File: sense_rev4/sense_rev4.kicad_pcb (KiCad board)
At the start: 2 copper layers, 68 x 52 mm, 46 parts, among them J1 Audio-Jack-4, P1 CONN_02X05, Q1 Q_PMOS_DGS, SW1 SW_SPST, U1 MDBT42Q, U2 PIR, U3 TLV8802, U4 MCP4012T-503E/CH, Y1 Crystal

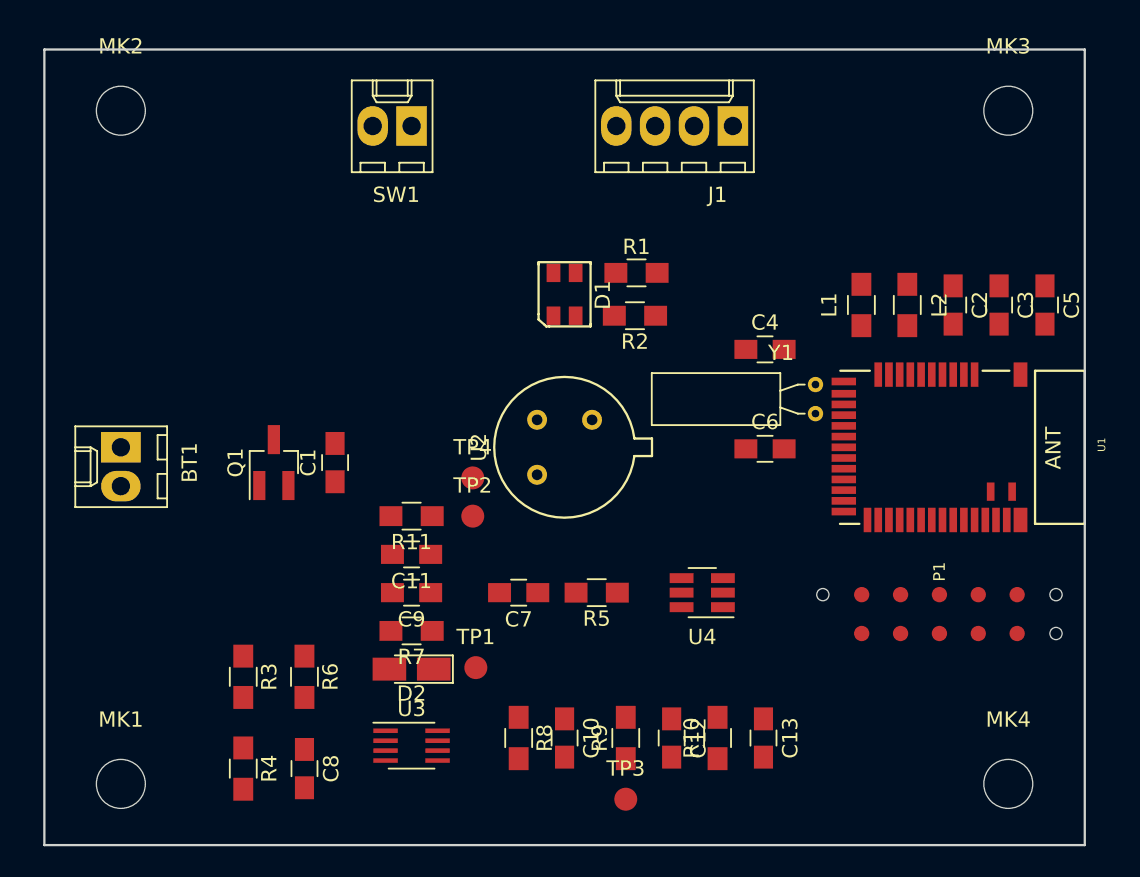
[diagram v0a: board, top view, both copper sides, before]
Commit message: Adds Schematics and PCB Layout files
PCB routing completed.
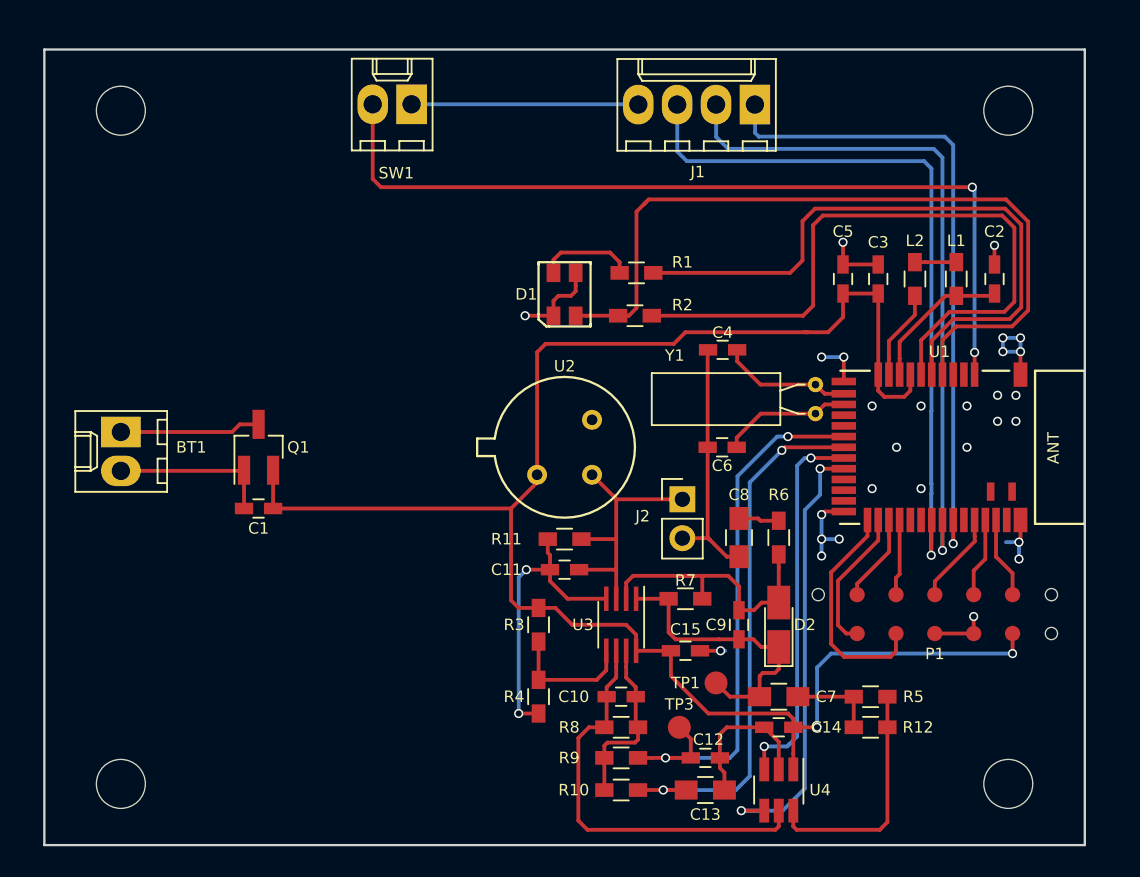
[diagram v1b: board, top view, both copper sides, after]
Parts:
- removed TP2, TP4: TEST, Measurement_Points:Measurement_Point_Round-SMD-Pad_Small
- added C14: 0.1uF, Capacitors_SMD:C_0603_HandSoldering, F.Cu at (152.0, 123.3)
- added C15: 0.1uF, Capacitors_SMD:C_0603_HandSoldering, F.Cu at (145.9, 118.3)
- added J2: Conn_01x02, Pin_Headers:Pin_Header_Straight_1x02_Pitch2.54mm, F.Cu at (145.7, 108.4)
- added R12: 33k, Resistors_SMD:R_0603_HandSoldering, F.Cu at (158.0, 123.3)
- C1, C10, C11, C2, C3, C4, C5, C6, C9: footprint Capacitors_SMD:C_0805_HandSoldering -> Capacitors_SMD:C_0603_HandSoldering
- C12: value 100nF -> 100pF; footprint Capacitors_SMD:C_0805_HandSoldering -> Capacitors_SMD:C_0603_HandSoldering
- C13, C7, C8: value 10uF -> 22uF
- L1, L2: footprint Inductors_SMD:L_0805_HandSoldering -> Inductors_SMD:L_0603_HandSoldering
- R1, R2: value R -> 22E; footprint Resistors_SMD:R_0805_HandSoldering -> Resistors_SMD:R_0603_HandSoldering
- R10, R6, R9: value 47k -> 33k; footprint Resistors_SMD:R_0805_HandSoldering -> Resistors_SMD:R_0603_HandSoldering
- R11, R3, R4, R7, R8: footprint Resistors_SMD:R_0805_HandSoldering -> Resistors_SMD:R_0603_HandSoldering
- R5: value 10k -> 33k; footprint Resistors_SMD:R_0805_HandSoldering -> Resistors_SMD:R_0603_HandSoldering
- moved R6 32.3 mm to (152.0, 110.9), turned to 90 degrees
- moved C8 32.2 mm to (149.4, 110.9)
- moved D2 24.2 mm to (152.0, 116.6), turned to 90 degrees
- moved C9 21.5 mm to (149.4, 116.6), turned to 90 degrees
- moved R4 19.9 mm to (136.3, 121.3)
- moved R3 19.6 mm to (136.3, 116.6)
- moved R5 19.1 mm to (158.0, 121.3)
- moved C7 18.3 mm to (152.0, 121.3)
- moved R7 18.0 mm to (145.9, 114.9), turned to 0 degrees
- moved U3 15.8 mm to (141.7, 116.6), turned to 270 degrees
- moved TP1 15.7 mm to (147.9, 120.4)
- moved U4 13.8 mm to (152.0, 127.4), turned to 270 degrees
- moved C5 13.3 mm to (156.2, 94.0)
- moved R11 10.1 mm to (138.0, 111.0)
- moved C11 10.0 mm to (138.0, 113.0)
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- renumbered MK1 to ?, MK2 to ?, MK3 to ?, MK4 to ?
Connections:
- P1 pad 10: GND -> /GPIO1
- P1 pad 2: /GPIO2 -> VDD
- P1 pad 4: VDD -> GND
- P1 pad 6: /GPIO1 -> GND
- P1 pad 8: /TX -> /GPIO2
- P1 pad 9: GND -> /TX
- R5 pad 1: Net-(R5-Pad1) -> Net-(R12-Pad1)
- U1 pad 17: /AMP_OFFSET -> /AMP_SIGNAL
- U1 pad 18: /AMP_SIGNAL -> /AMP_OFFSET
- U1 pad 2: Net-(U1-Pad2) -> /BUTTON
- U1 pad 25: /TRIGGER -> /GPIO2
- U1 pad 26: /FOCUS -> /GPIO1
- U1 pad 27: /AUDIO_JACK_IO -> /TX
- U1 pad 28: Net-(U1-Pad28) -> /RX
- U1 pad 3: /BUTTON -> Net-(U1-Pad3)
- U1 pad 31: /GPIO2 -> /AUDIO_JACK_IO
- U1 pad 32: /GPIO1 -> /FOCUS
- U1 pad 33: /TX -> /TRIGGER
- U1 pad 34: /RX -> Net-(U1-Pad34)
- U1 pad 4: /LED_RED -> Net-(U1-Pad4)
- U1 pad 5: /LED_GREEN -> /LED_SENSE
- U1 pad 6: /LED_SENSE -> /LED_RED
- U1 pad 7: Net-(U1-Pad7) -> /LED_GREEN
- U4 pad 5: Net-(R5-Pad1) -> Net-(C10-Pad2)
- U4 pad 6: Net-(C10-Pad2) -> Net-(R12-Pad1)
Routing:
- net VDD: track 0.00 -> 116.2 mm, vias 0 -> 2
- net GND: track 0.00 -> 105.0 mm, vias 0 -> 19
- net /BUTTON: track 0.00 -> 56.6 mm, vias 0 -> 2
- net /LED_SENSE: track 0.00 -> 51.7 mm
- net /AUDIO_JACK_IO: track 0.00 -> 47.8 mm, vias 0 -> 1
- net /FOCUS: track 0.00 -> 45.1 mm, vias 0 -> 1
- net /LED_GREEN: track 0.00 -> 44.0 mm
- net /TRIGGER: track 0.00 -> 42.7 mm, vias 0 -> 1
- net /LED_RED: track 0.00 -> 42.1 mm
- net /AMP_SIGNAL: track 0.00 -> 36.8 mm, vias 0 -> 2
- net /AMP_OFFSET: track 0.00 -> 35.5 mm, vias 0 -> 2
- net /MCP4012T_CS: track 0.00 -> 29.1 mm, vias 0 -> 2
- net Net-(C10-Pad2): track 0.00 -> 27.2 mm
- net /MCP4012T_U/d: track 0.00 -> 25.0 mm, vias 0 -> 2
- net /OUT_A: track 0.00 -> 19.4 mm
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- added copper zone on B.Cu, net GND

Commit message: Updated PCB Routing
PCB routing updated,
Appiko, OSHW and KiCAD logos added.
All component placement changed.
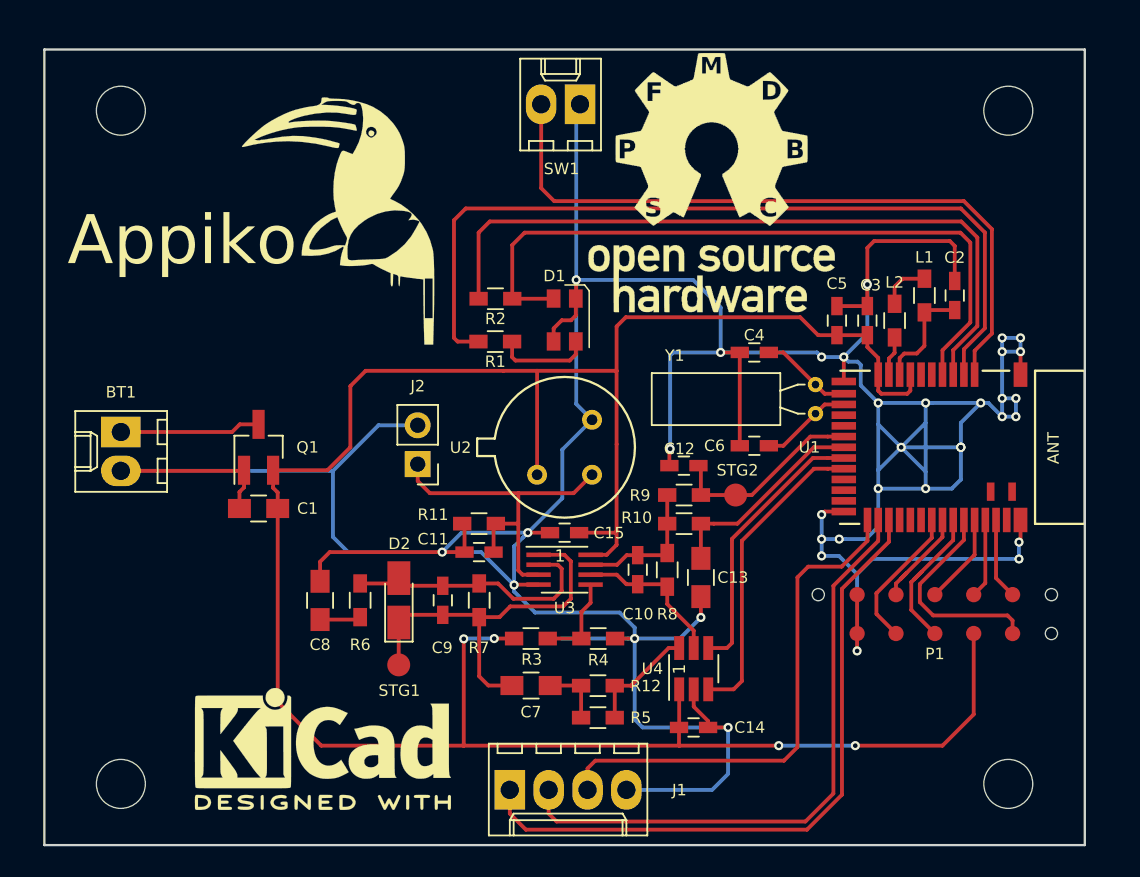
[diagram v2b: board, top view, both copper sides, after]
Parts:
- added ?: , sense_rev3_fp:LOGO, F.Cu at (123.2, 90.2)
- added ?: KiCad-Logo2_8mm_SilkScreen, sense_rev3_fp:KiCad-Logo2_8mm_SilkScreen, F.Cu at (122.2, 124.7)
- added G***: LOGO, sense_rev3_fp:OSHW1, F.Cu at (147.6, 87.7)
- C1: footprint Capacitors_SMD:C_0603_HandSoldering -> Capacitors_SMD:C_0805_HandSoldering
- moved J1 47.6 mm to (134.4, 127.4), turned to 0 degrees
- moved C8 27.7 mm to (122.0, 115.0), turned to 90 degrees
- moved R6 27.7 mm to (124.6, 115.0), turned to 270 degrees
- moved D2 24.9 mm to (127.2, 115.0)
- moved STG1 20.8 mm to (127.2, 119.2)
- moved C9 19.4 mm to (130.0, 115.0)
- moved C12 19.2 mm to (145.8, 106.2), turned to 0 degrees
- moved R12 18.0 mm to (140.2, 120.6)
- moved R10 17.9 mm to (145.8, 110.0)
- moved R5 17.9 mm to (140.2, 122.7)
- moved R9 17.7 mm to (145.8, 108.1)
- moved J2 17.5 mm to (128.4, 106.1), turned to 180 degrees
- moved C7 16.2 mm to (135.8, 120.6)
- moved STG2 15.6 mm to (149.2, 108.1)
- moved C13 13.9 mm to (146.9, 113.5), turned to 90 degrees
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- renumbered TP1 to STG1, TP3 to STG2
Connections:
- P1 pad 10: /GPIO1 -> GND
- P1 pad 2: VDD -> /TX
- P1 pad 4: GND -> VDD
- P1 pad 6: GND -> /GPIO1
- P1 pad 7: /RX -> /GPIO2
- P1 pad 8: /GPIO2 -> /RX
- P1 pad 9: /TX -> GND
- U1 pad 25: /GPIO2 -> /AUDIO_JACK_IO
- U1 pad 26: /GPIO1 -> /FOCUS
- U1 pad 27: /TX -> /TRIGGER
- U1 pad 28: /RX -> Net-(U1-Pad28)
- U1 pad 3: Net-(U1-Pad3) -> /LED_RED
- U1 pad 31: /AUDIO_JACK_IO -> /RX
- U1 pad 32: /FOCUS -> /GPIO2
- U1 pad 33: /TRIGGER -> /GPIO1
- U1 pad 34: Net-(U1-Pad34) -> /TX
- U1 pad 4: Net-(U1-Pad4) -> /LED_GREEN
- U1 pad 6: /LED_RED -> Net-(U1-Pad6)
- U1 pad 7: /LED_GREEN -> Net-(U1-Pad7)
- U4 pad 3: /MCP4012T_U/d -> /MCP4012T_CS
- U4 pad 4: /MCP4012T_CS -> /MCP4012T_U/d
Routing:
- net GND: track 105.0 -> 315.2 mm, vias 19 -> 35
- net VDD: track 116.2 -> 159.9 mm, vias 2 -> 4
- net /AMP_SIGNAL: track 36.8 -> 12.9 mm, vias 2 -> 0
- net /AMP_OFFSET: track 35.5 -> 13.7 mm, vias 2 -> 0
- net Net-(C10-Pad2): track 27.2 -> 10.1 mm
- net /AUDIO_JACK_IO: track 47.8 -> 33.7 mm, vias 1 -> 0
- net /LED_RED: track 42.1 -> 54.9 mm
- net /BUTTON: track 56.6 -> 46.0 mm, vias 2 -> 0
- net /MCP4012T_CS: track 29.1 -> 20.2 mm, vias 2 -> 0
- net /GPIO2: track 15.0 -> 6.65 mm
- net Net-(R12-Pad1): track 15.7 -> 7.32 mm
- net /TX: track 5.75 -> 14.0 mm
- net /MCP4012T_U/d: track 25.0 -> 18.0 mm, vias 2 -> 0
- net /OUT_A: track 19.4 -> 25.8 mm
- net /LED_SENSE: track 51.7 -> 46.1 mm
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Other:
- net class Default: via_drill 0.4 -> 0.35
- rule via_min_drill: 0.3 -> 0.2
- board text added: "1"

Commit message: Updates PCB files
Added notes in schematic, and changes few references in PCB file.
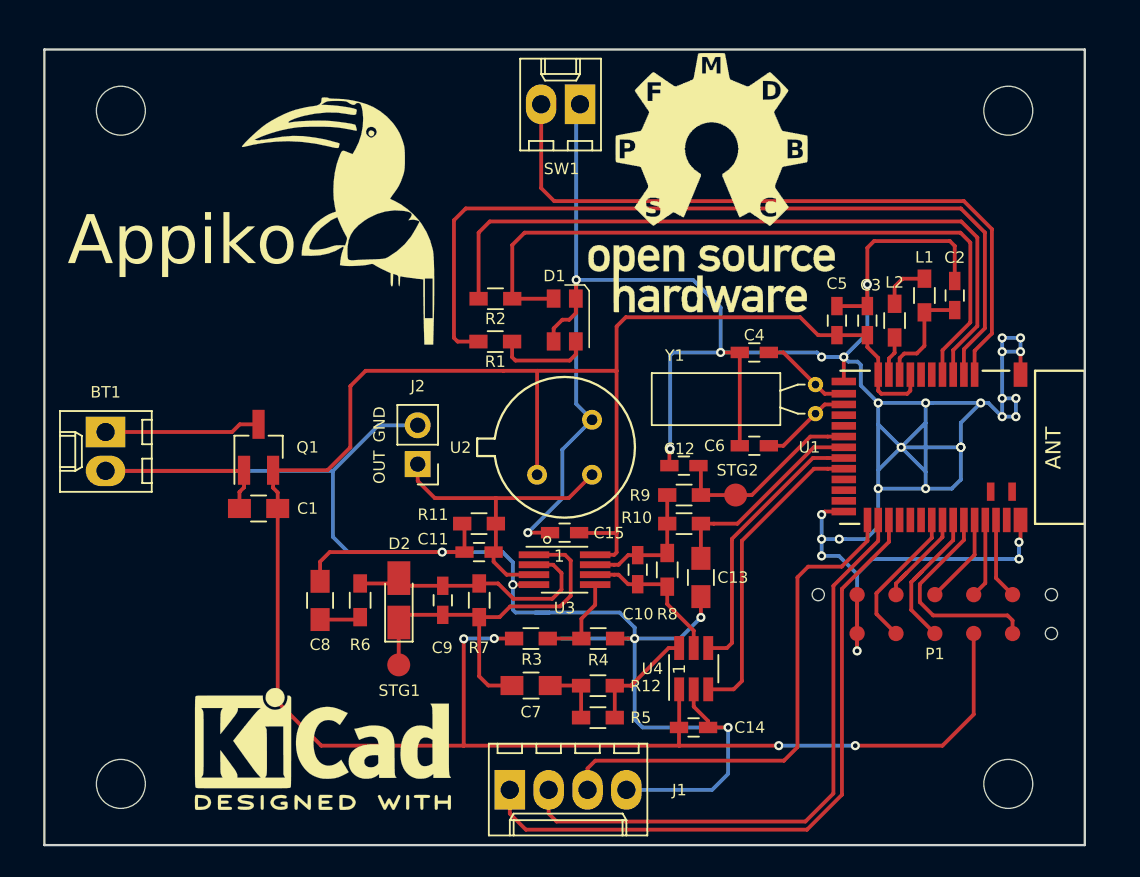
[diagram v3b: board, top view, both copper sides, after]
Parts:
- U3: footprint Housings_SSOP:SSOP-8_2.95x2.8mm_Pitch0.65mm -> sense_rev3_fp:SSOP-8_2.95x2.8mm_Pitch0.65mm_Hand_Soldering
- moved BT1 1.00 mm to (108.0, 104.0)
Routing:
- net GND: track 315.2 -> 309.5 mm
- net /PIR_OUT: track 23.2 -> 20.8 mm
- net Net-(BT1-Pad1): track 9.21 -> 10.2 mm
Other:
- board text added: "GND"
- board text added: "OUT"
